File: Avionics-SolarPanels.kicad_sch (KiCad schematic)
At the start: 6 parts

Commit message: v3.1 Updates
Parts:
- H1, H4: footprint MountingHole:MountingHole_3.2mm_M3_DIN965_Pad_TopBottom -> Argus-Miscellaneous:MountingHole_3.2mm_5.2mm_Slot_TopBottom
- H5, H6: footprint MountingHole:MountingHole_3mm_Pad_TopBottom -> MountingHole:MountingHole_2.2mm_M2_DIN965_Pad_TopOnly
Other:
- company: (none) -> Carnegie Mellon University
- title: (none) -> Argus XY Solar Panel
- moved on the sheet: H1, H2, H3, H4, H5, H6

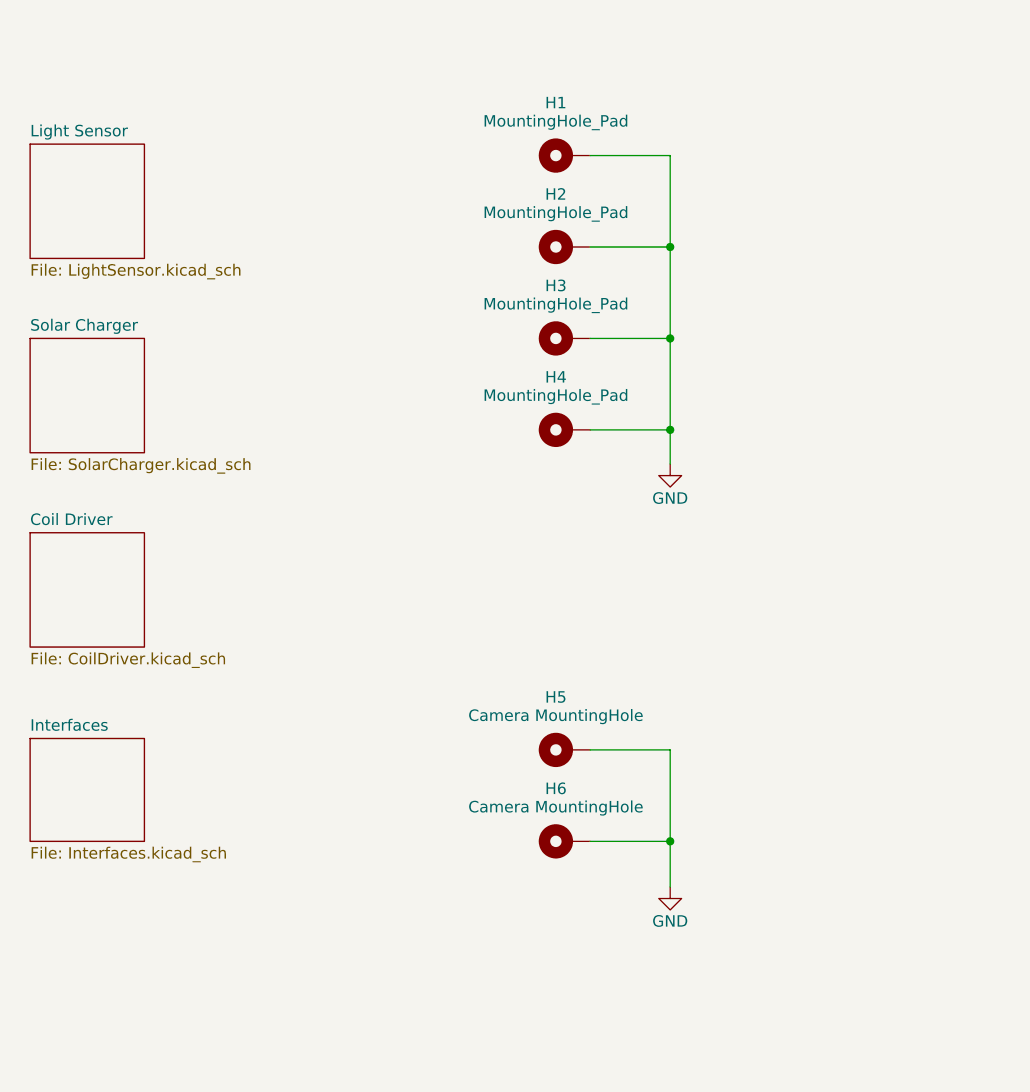
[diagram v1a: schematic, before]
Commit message: Updated access port, added deployment sensor
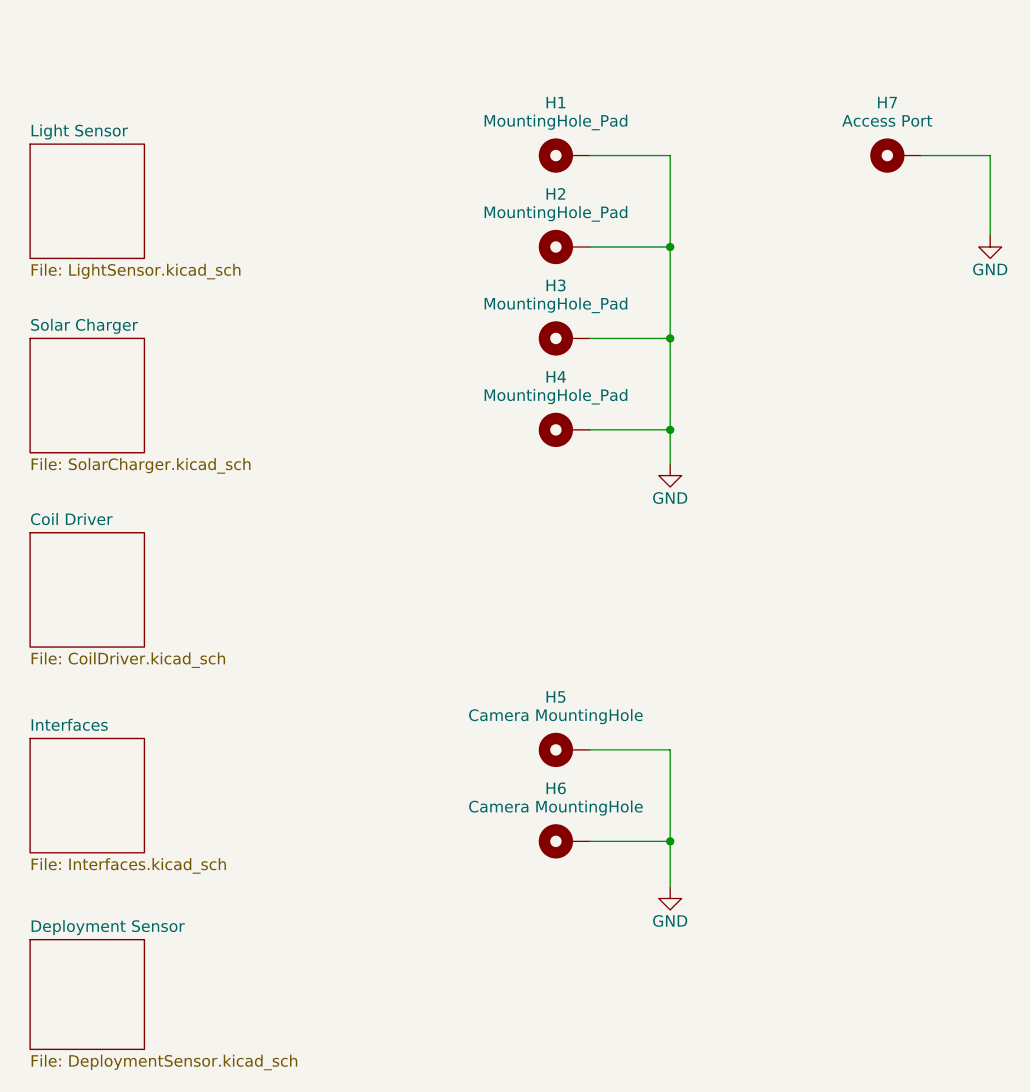
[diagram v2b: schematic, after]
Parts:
- added H7: Access Port, Argus-Miscellaneous:Access Port 2, symbol Mechanical:MountingHole_Pad
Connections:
- net GND: now also H7.1
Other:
- added sheet Deployment Sensor (DeploymentSensor.kicad_sch)
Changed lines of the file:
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@@
+	(wire
+		(pts
+			(xy 218.44 60.96) (xy 218.44 69.85)
+		)
+		(stroke
+			(width 0)
+			(type default)
+		)
+	)
 	(wire
 		(pts
@@
 	(wire
 		(pts
+			(xy 210.82 60.96) (xy 218.44 60.96)
+		)
+		(stroke
+			(width 0)
+			(type default)
+		)
+	)
+	(wire
+		(pts
 			(xy 182.88 91.44) (xy 182.88 95.25)
 		)
@@
 	(symbol
 		(lib_id "Mechanical:MountingHole_Pad")
-		(at 171.45 127 90)
+		(at 208.28 60.96 90)
 		(unit 1)
 		(exclude_from_sim yes)
@@
 		(on_board yes)
 		(dnp no)
+		(property "Reference" "H7"
+			(at 207.01 55.118 90)
+			(effects
+				(font
+					(size 1.27 1.27)
+				)
+			)
+		)
+		(property "Value" "Access Port"
+			(at 207.01 57.15 90)
+			(effects
+				(font
+					(size 1.27 1.27)
+				)
+			)
+		)
+		(property "Footprint" "Argus-Miscellaneous:Access Port 2"
+			(at 208.28 60.96 0)
+			(effects
+				(font
+					(size 1.27 1.27)
+				)
+				(hide yes)
+			)
+		)
+		(property "Datasheet" "~"
+			(at 208.28 60.96 0)
+			(effects
+				(font
+					(size 1.27 1.27)
+				)
+				(hide yes)
+			)
+		)
+		(property "Description" "Mounting Hole with connection"
+			(at 208.28 60.96 0)
+			(effects
+				(font
+					(size 1.27 1.27)
+				)
+				(hide yes)
+			)
+		)
+		(pin "1"
+		)
+		(instances
+			(project "Avionics-SolarPanels"
+				(path "/92e58b76-9357-4452-b231-18fffdf58e73"
+					(reference "H7")
+					(unit 1)
+				)
+			)
+		)
+	)
+	(symbol
+		(lib_id "Mechanical:MountingHole_Pad")
+		(at 171.45 127 90)
+		(unit 1)
+		(exclude_from_sim yes)
+		(in_bom no)
+		(on_board yes)
+		(dnp no)
 		(property "Reference" "H5"
 			(at 170.18 121.158 90)
@@
 				(path "/92e58b76-9357-4452-b231-18fffdf58e73"
 					(reference "#PWR017")
+					(unit 1)
+				)
+			)
+		)
+	)
+	(symbol
+		(lib_id "power:GND")
+		(at 218.44 69.85 0)
+		(unit 1)
+		(exclude_from_sim no)
+		(in_bom yes)
+		(on_board yes)
+		(dnp no)
+		(property "Reference" "#PWR060"
+			(at 218.44 76.2 0)
+			(effects
+				(font
+					(size 1.27 1.27)
+				)
+				(hide yes)
+			)
+		)
+		(property "Value" "GND"
+			(at 218.44 73.66 0)
+			(effects
+				(font
+					(size 1.27 1.27)
+				)
+			)
+		)
+		(property "Footprint" ""
+			(at 218.44 69.85 0)
+			(effects
+				(font
+					(size 1.27 1.27)
+				)
+				(hide yes)
+			)
+		)
+		(property "Datasheet" ""
+			(at 218.44 69.85 0)
+			(effects
+				(font
+					(size 1.27 1.27)
+				)
+				(hide yes)
+			)
+		)
+		(property "Description" "Power symbol creates a global label with name \"GND\" , ground"
+			(at 218.44 69.85 0)
+			(effects
+				(font
+					(size 1.27 1.27)
+				)
+				(hide yes)
+			)
+		)
+		(pin "1"
+		)
+		(instances
+			(project "Avionics-SolarPanels"
+				(path "/92e58b76-9357-4452-b231-18fffdf58e73"
+					(reference "#PWR060")
 					(unit 1)
 				)
@@
 	(sheet
 		(at 111.76 125.73)
-		(size 12.7 11.43)
+		(size 12.7 12.7)
 		(exclude_from_sim no)
 		(in_bom yes)
@@
 		)
 		(property "Sheetfile" "Interfaces.kicad_sch"
-			(at 111.76 137.7446 0)
+			(at 111.76 139.0146 0)
 			(effects
 				(font
@@
 				)
 			)
+		)
+	)
+	(sheet
+		(at 111.76 148.082)
+		(size 12.7 12.192)
+		(exclude_from_sim no)
+		(in_bom yes)
+		(on_board yes)
+		(dnp no)
+		(fields_autoplaced yes)
+		(stroke
+			(width 0.1524)
+			(type solid)
+		)
+		(fill
+			(color 0 0 0 0.0000)
+		)
+		(property "Sheetname" "Deployment Sensor"
+			(at 111.76 147.3704 0)
+			(effects
+				(font
+					(size 1.27 1.27)
+				)
+				(justify left bottom)
+			)
+		)
+		(property "Sheetfile" "DeploymentSensor.kicad_sch"
+			(at 111.76 160.8586 0)
+			(effects
+				(font
+					(size 1.27 1.27)
+				)
+				(justify left top)
+			)
+		)
+		(instances
+			(project "Avionics-SolarPanels"
+				(path "/92e58b76-9357-4452-b231-18fffdf58e73"
+					(page "18")
+				)
+			)
